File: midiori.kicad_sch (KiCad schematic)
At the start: 94 parts, among them J1 midiori-rescue_x68000_expansi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, J2 Conn_ARM_JTAG_SWD_10, J3 AudioJack3, J4 Mini-DIN-5, J5 AudioJack3, J6 AudioJack3, J7 Conn_01x06, J8 AudioJack3, J9 Mini-DIN-5, U1 74lv07, U10 ICE40HX1K-TQ144, U11 AP2205K-3.3, U12 AK4432, U13 TL072, U14 AP2205K-3.3, U15 TL072, U16 74lv07, U17 H11L1, U18 SN74LVC245APW, U19 74lv07, U2 AT25SF081-SSHD-X, U3 AP2127K-1.2, U4 SN74LVC245APW, U5 SN74LVC245APW, U6 SN74LVC245APW, U7 SN74LVC245APW, U8 SN74LVC245APW, U9 SN74LVC245APW, X1 16MHz, X2 24.576MHz

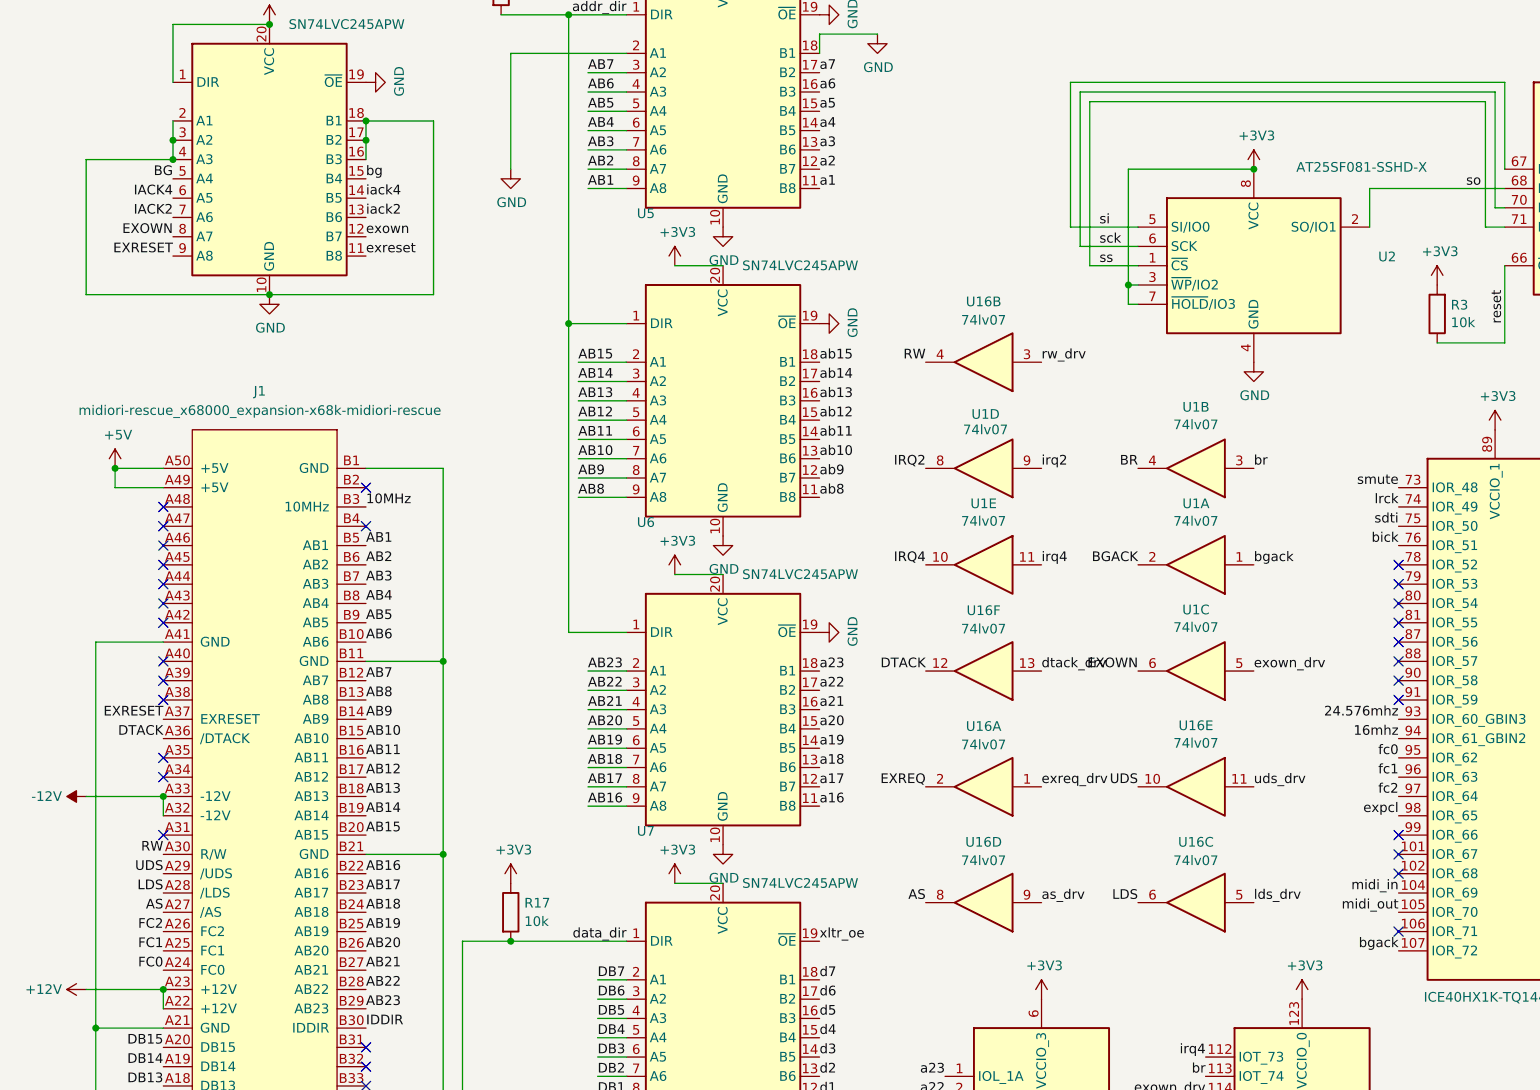
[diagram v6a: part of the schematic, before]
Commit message: add bgack readback pin
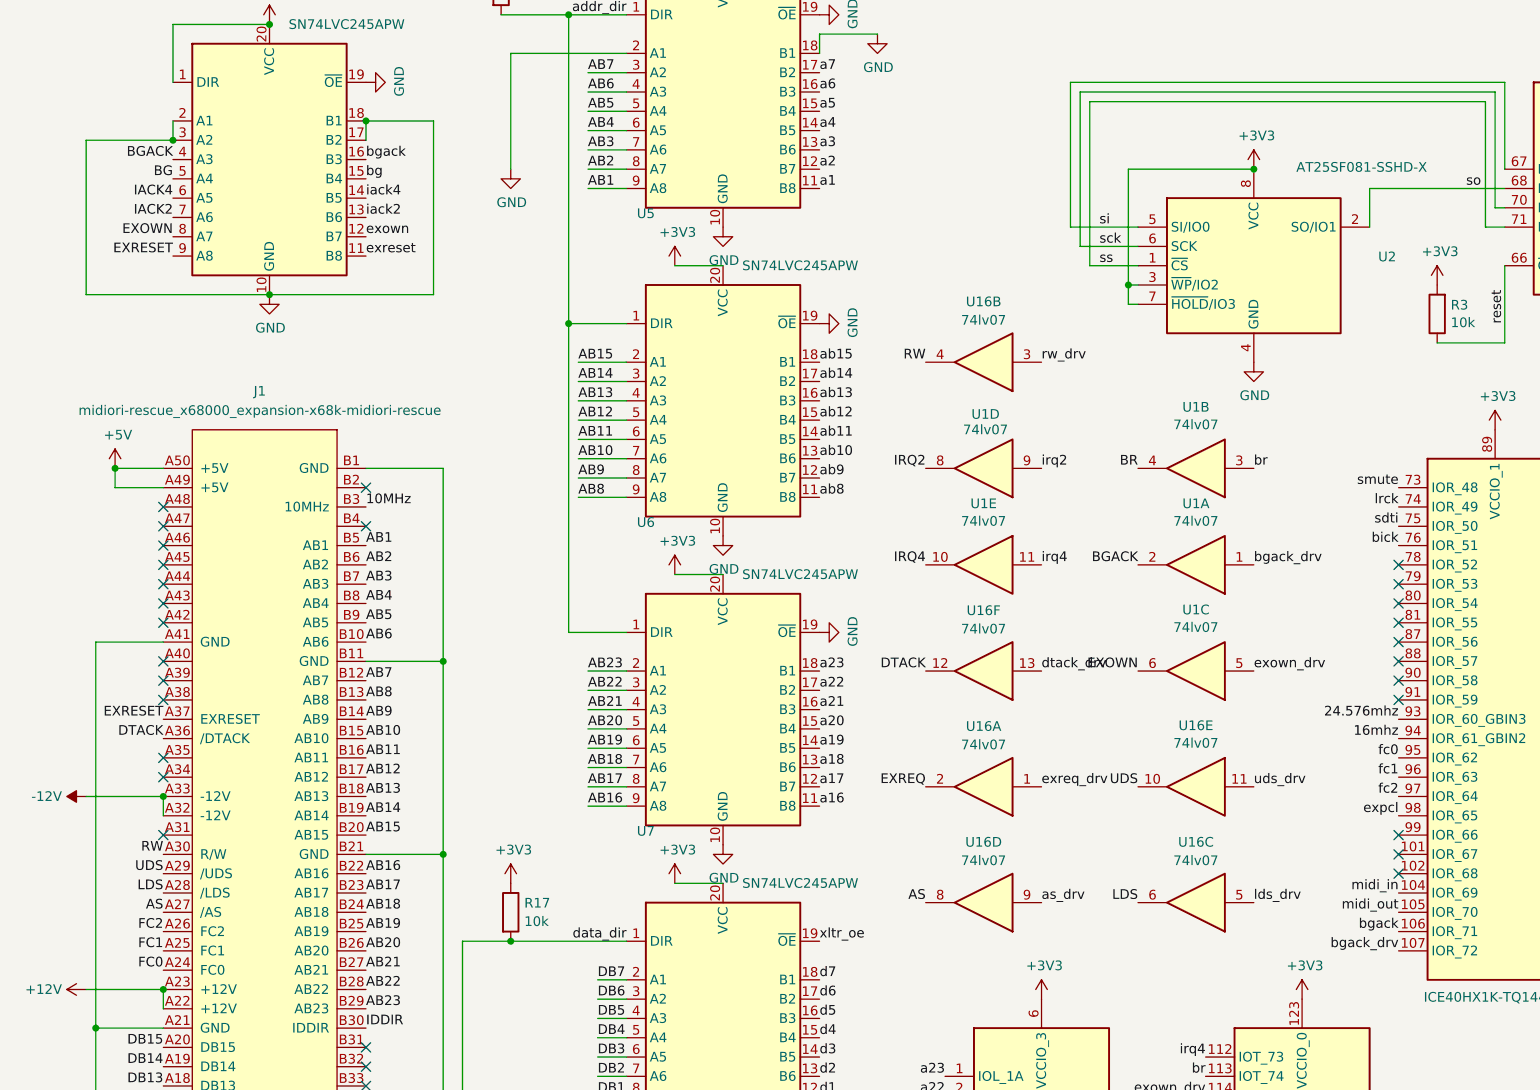
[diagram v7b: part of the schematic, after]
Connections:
- net BGACK: now also U18.4 (A3)
- net GND: no longer U18.16 (B3), U18.4 (A3)
- net bgack: now also U10.106 (IOR_71), U18.16 (B3); no longer U1.1, U10.107 (IOR_72)
- new net bgack_drv: U1.1, U10.107 (IOR_72)
- no-connect marks 43 -> 42
